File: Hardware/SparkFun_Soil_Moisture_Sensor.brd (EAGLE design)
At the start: 22.9 x 61 mm, 27 parts, among them J1 GATORGATOR_MINI, J2 GATORGATOR_MINI, J3 GATORGATOR_MINI, Q1 2N3904

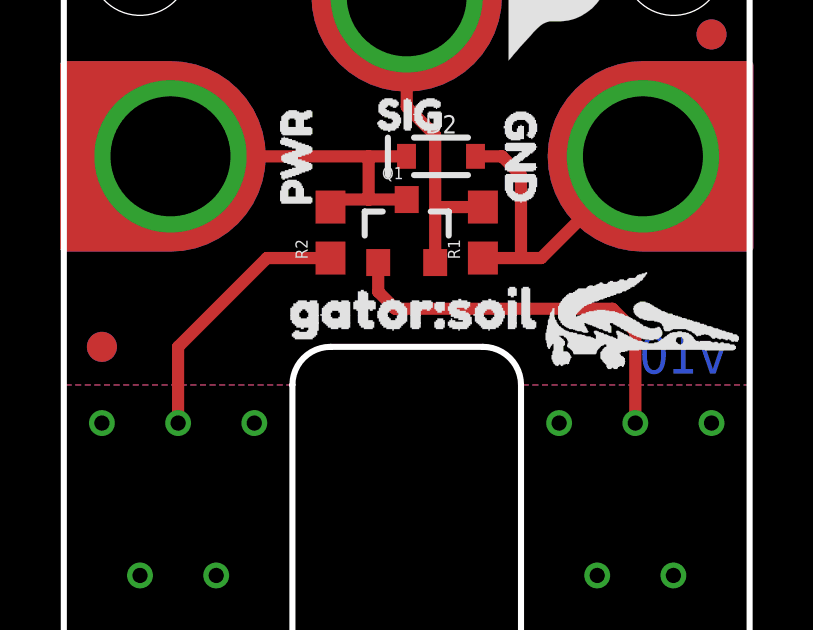
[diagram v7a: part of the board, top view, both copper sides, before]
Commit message: centering gator silk
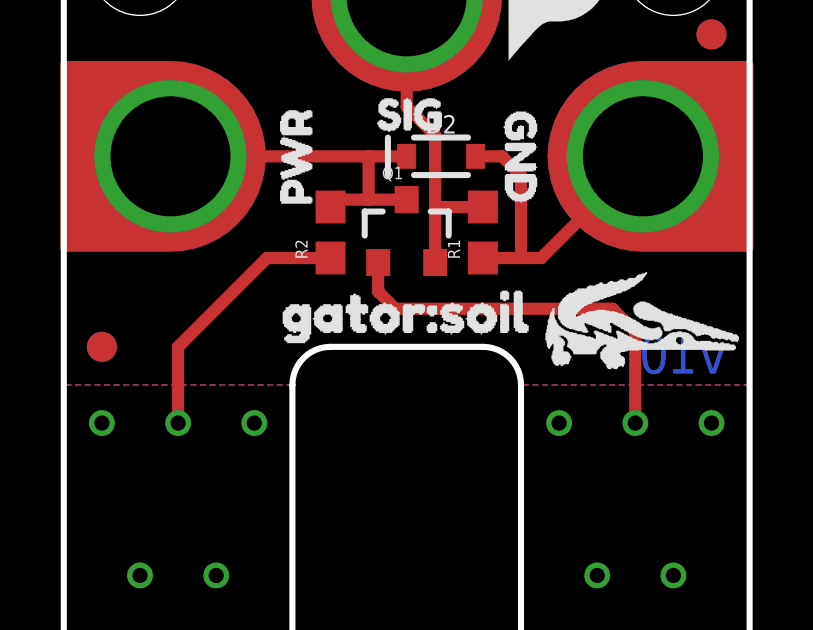
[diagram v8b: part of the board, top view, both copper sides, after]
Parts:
- moved U$8 0.28 mm to (6.10, 46.9)
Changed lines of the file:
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@@
 <element name="U$10" library="SparkFun-Aesthetics" package="ORDERING_INSTRUCTIONS" value="" x="-6.35" y="-16.51"/>
 <element name="U$11" library="GatorBit_Final_for_Silk#01#png (3)" package="GATORBIT_FINAL_FOR_SILK#01#PNG" value="" x="19.304" y="46.609"/>
-<element name="U$8" library="buzzard_labels (16)" package="GATOR#SOIL1" value="" x="6.35" y="46.99"/>
+<element name="U$8" library="buzzard_labels (16)" package="GATOR#SOIL1" value="" x="6.096" y="46.863"/>
 </elements>
 <signals>
